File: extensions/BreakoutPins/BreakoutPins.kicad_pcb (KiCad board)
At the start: 2 copper layers, 42 x 27 mm, 8 parts, among them M1 MH_M3, M2 MH_M3, M3 MH_M3, M4 MH_M3, P1 Smoothie-teer-Daisy, P2 CONN_01X10, P3 Smoothie-teer-Daisy

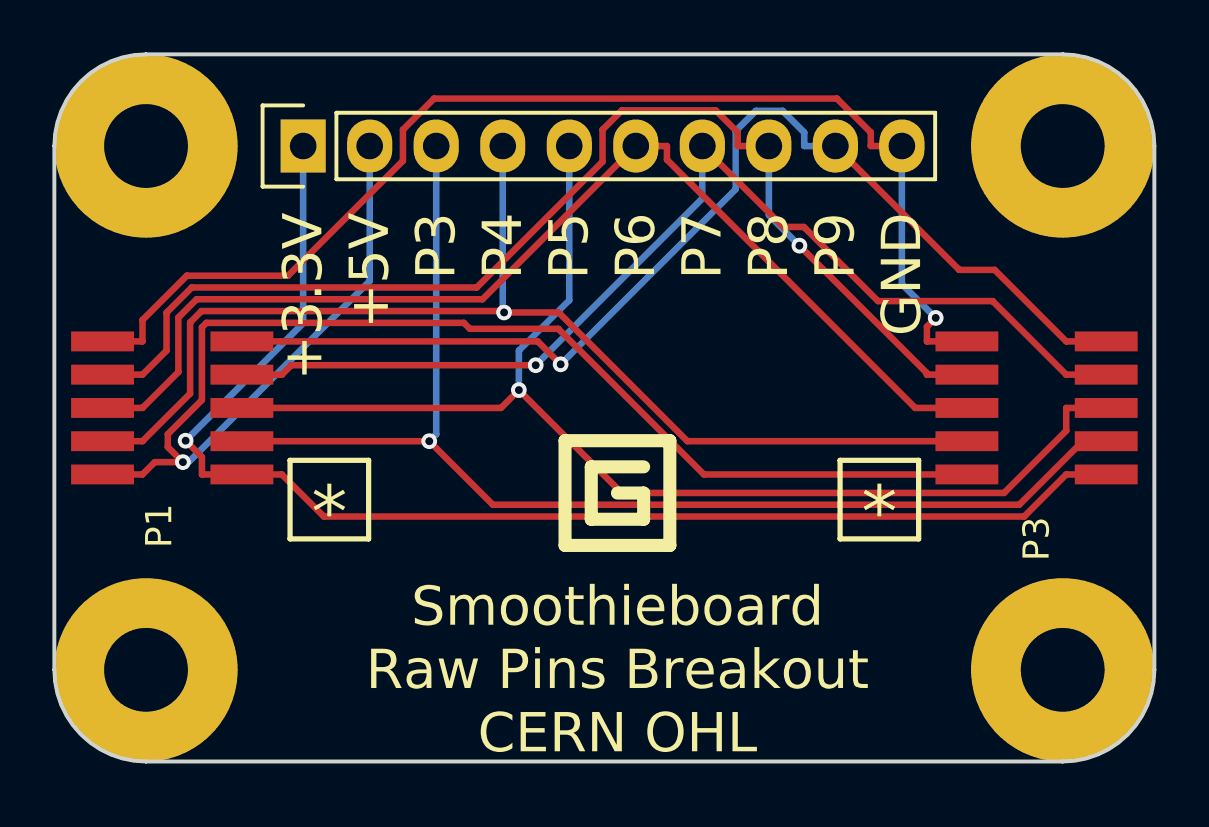
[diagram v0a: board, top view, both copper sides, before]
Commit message: Update to BreakoutPins
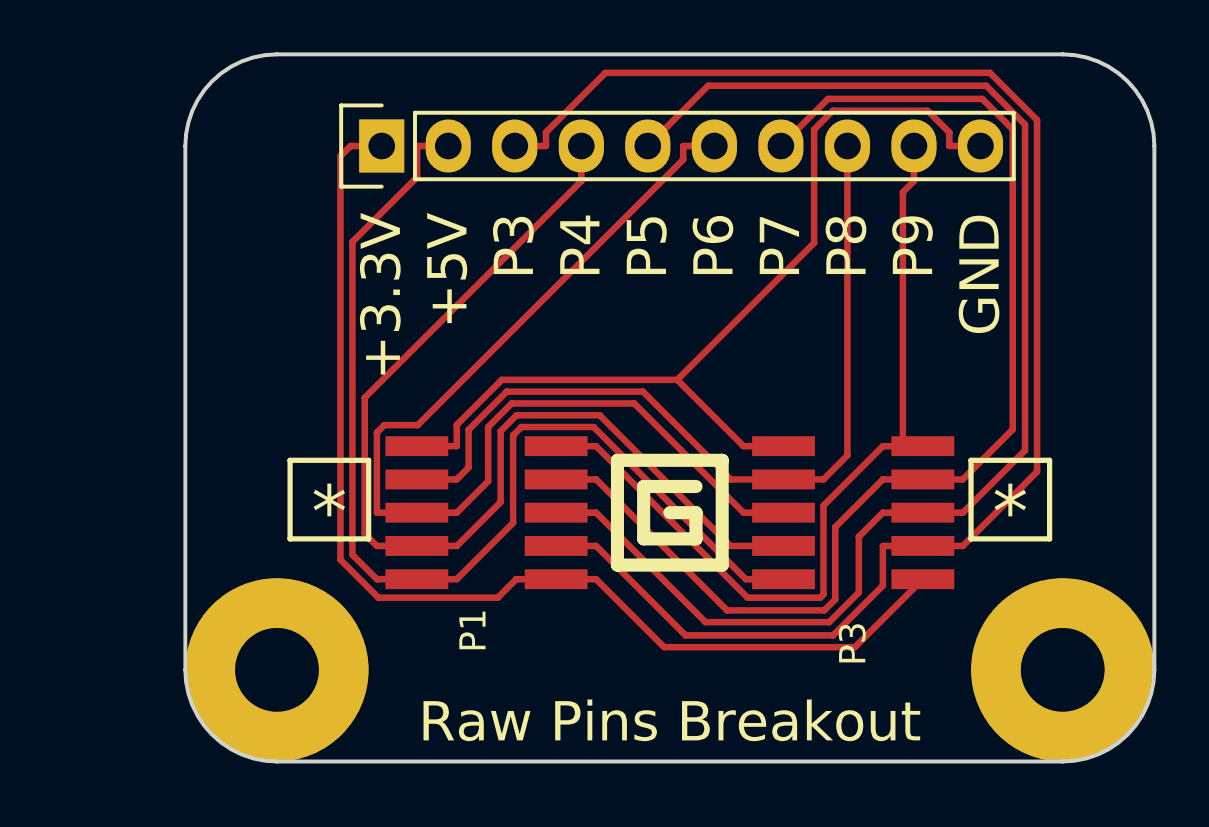
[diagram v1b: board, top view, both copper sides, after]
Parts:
- removed M3, M4: MH_M3, SBV2_Footprints:M3_Mounting_Hole
- moved P1 12.6 mm to (138.0, 99.0)
- moved P3 8.06 mm to (152.0, 99.0)
- moved M1 5.00 mm to (130.0, 105.0)
- moved P2 3.00 mm to (134.0, 85.0)
- moved G*** 2.14 mm to (145.0, 99.0)
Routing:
- net /P2: track 56.0 -> 41.4 mm, vias 1 -> 0
- net /P8: track 44.8 -> 32.3 mm, vias 1 -> 0
- net /P3: track 46.4 -> 58.8 mm, vias 1 -> 0
- net GND: track 46.2 -> 35.8 mm, vias 1 -> 0
- net /P9: track 42.6 -> 32.4 mm, vias 1 -> 0
- net /P1: track 50.5 -> 42.4 mm, vias 1 -> 0
- net /P5: track 46.9 -> 52.0 mm, vias 1 -> 0
- net /P4: track 45.1 -> 40.1 mm, vias 1 -> 0
- net /P7: track 41.4 -> 45.5 mm, vias 1 -> 0
- net /P6: track 42.8 -> 41.0 mm
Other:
- board size 42 x 27 mm -> 37 x 27 mm
- board text added: "Raw Pins Breakout"
- board text removed: "Smoothieboard Raw Pins Breakout CERN OHL"
